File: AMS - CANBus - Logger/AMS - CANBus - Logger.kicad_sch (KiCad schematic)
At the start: 12 parts, among them IC4 CD74HC4050ME4, IC5 AZ1117CH2-3.3TRG1, J1 Power_And_CAN, Q1 IRF9Z34NPBF, U5 3568

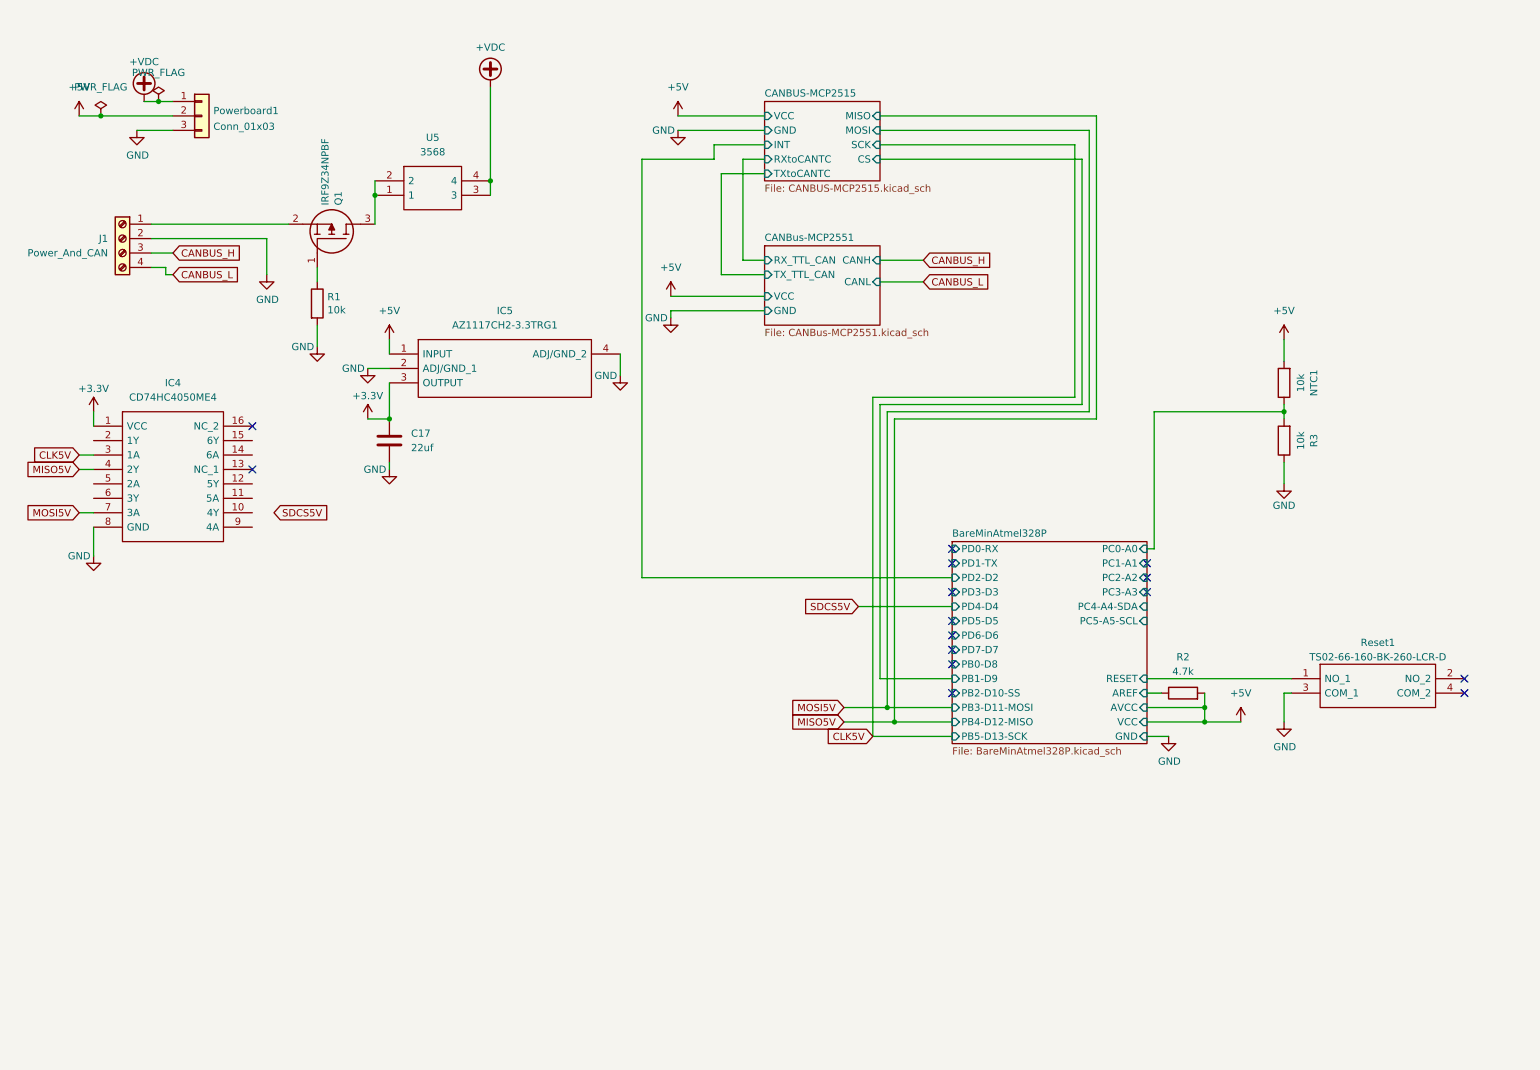
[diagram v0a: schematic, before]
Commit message: finished the regular format adding the uno shield
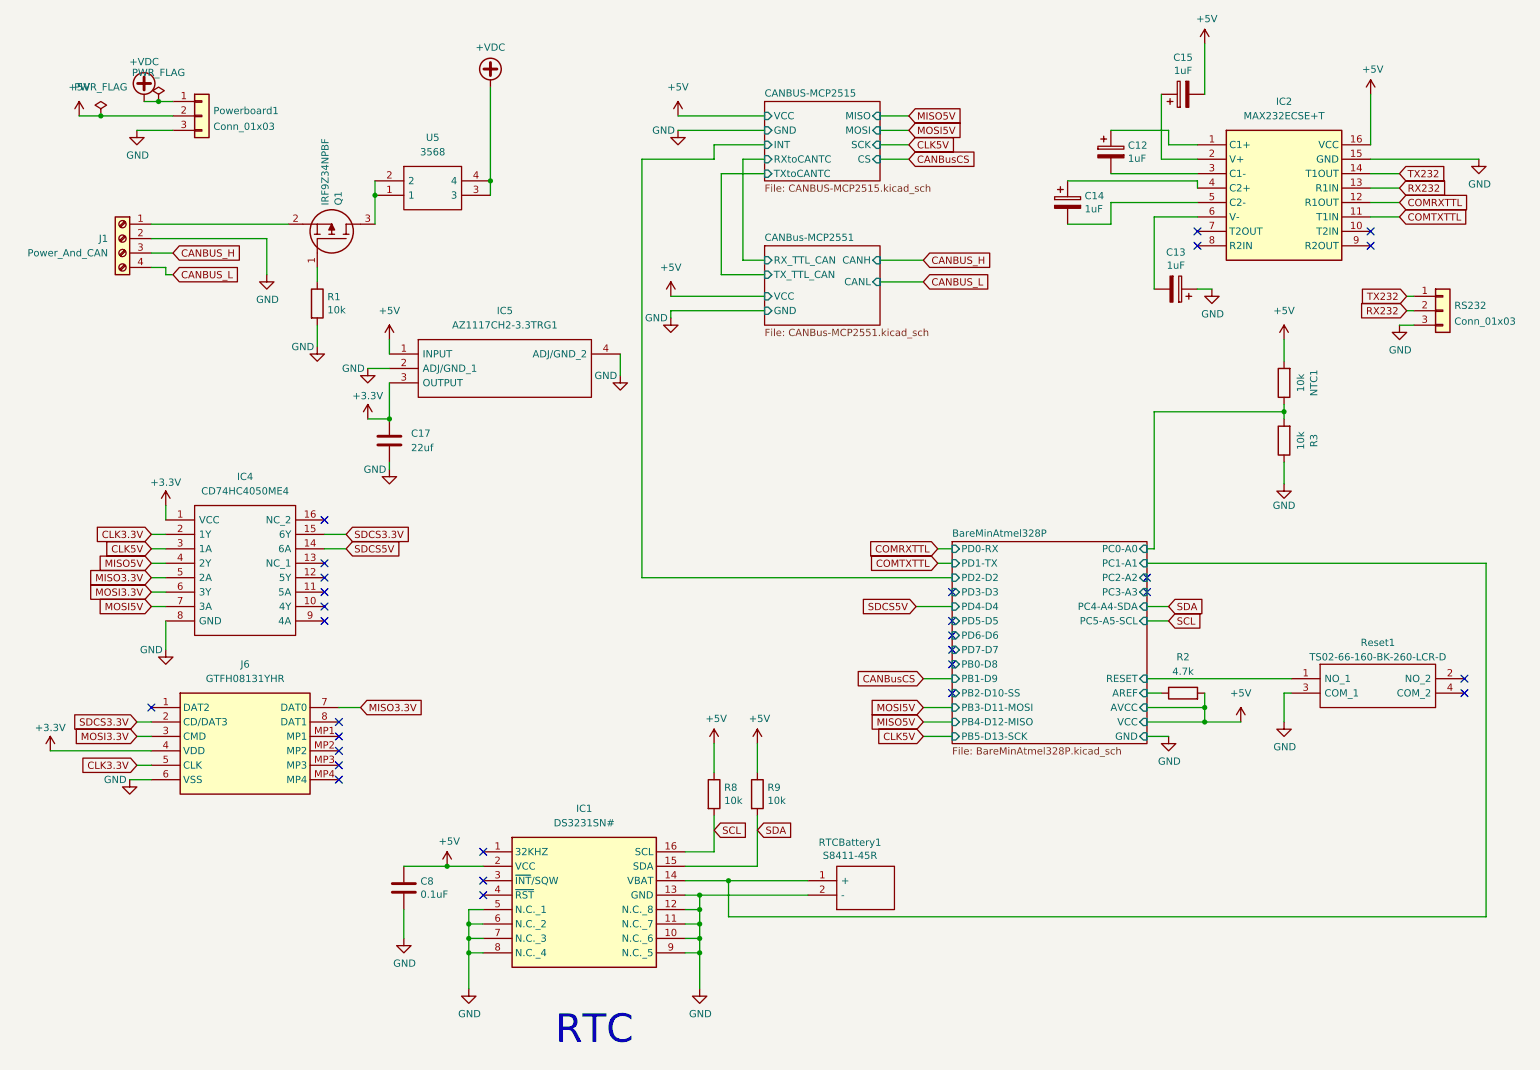
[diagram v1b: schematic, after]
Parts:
- added C12, C13, C14, C15: 1uF, Capacitor_THT:CP_Radial_D5.0mm_P2.50mm, symbol Device:CP
- added C8: 0.1uF, Capacitor_SMD:C_1206_3216Metric_Pad1.33x1.80mm_HandSolder, symbol Device:C
- added IC1: DS3231SN#, SOIC127P1032X265-16N, symbol SamacSys:DS3231SN#
- added IC2: MAX232ECSE+T, SOIC127P600X175-16N, symbol SamacSys:MAX232ECSE+T
- added J6: GTFH08131YHR, GTFH08131YHR, symbol SamacSys:GTFH08131YHR
- added R8, R9: 10k, Resistor_SMD:R_1206_3216Metric_Pad1.30x1.75mm_HandSolder, symbol Device:R
- added RS232: Conn_01x03, Connector_PinHeader_2.54mm:PinHeader_1x03_P2.54mm_Vertical, symbol Connector_Generic:Conn_01x03
- added RTCBattery1: S8411-45R, SamacSys_Parts:S8411-45R_1, symbol SamacSys_Parts:S8411-45R
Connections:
- net +3.3V: now also J6.4 (VDD)
- net +5V: now also C15.2, C8.1, IC1.2 (VCC), IC2.16 (VCC), R8.1, R9.1
- net BareMinAtmel328P/PC1-A1: now also IC1.14 (VBAT), RTCBattery1.1 (+)
- net GND: now also C13.1, C8.2, IC1.10 (N.C._6), IC1.11 (N.C._7), IC1.12 (N.C._8), IC1.13 (GND), IC1.5 (N.C._1), IC1.6 (N.C._2), IC1.7 (N.C._3), IC1.8 (N.C._4), IC1.9 (N.C._5), IC2.15 (GND), J6.6 (VSS), RS232.3 (Pin_3), RTCBattery1.2 (-)
- net SDCS5V: now also IC4.14 (6A)
- net SDCS3.3V: now reaches IC4.15 (6Y)
- net SDCS3.3V: now also J6.2 (CD/DAT3)
- net CLK3.3V: now reaches IC4.2 (1Y)
- net CLK3.3V: now also J6.5 (CLK)
- net MISO3.3V: now reaches IC4.5 (2A)
- net MISO3.3V: now also J6.7 (DAT0)
- net MOSI3.3V: now reaches IC4.6 (3Y)
- net MOSI3.3V: now also J6.3 (CMD)
- new net: C14.1, IC2.4 (C2+)
- new net: C14.2, IC2.5 (C2-)
- new net: C12.1, IC2.1 (C1+)
- new net: C12.2, IC2.3 (C1-)
- new net: C15.1, IC2.2 (V+)
- new net: C13.2, IC2.6 (V-)
- new net COMRXTTL: IC2.12 (R1OUT)
- new net COMTXTTL: IC2.11 (T1IN)
- new net RX232: IC2.13 (R1IN), RS232.2 (Pin_2)
- new net SCL: IC1.16 (SCL), R8.2
- new net SDA: IC1.15 (SDA), R9.2
- new net TX232: IC2.14 (T1OUT), RS232.1 (Pin_1)
- no-connect marks 15 -> 29
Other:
- note added: "RTC"
- moved on the sheet: IC4
